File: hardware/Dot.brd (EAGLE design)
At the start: 25.4 x 31.5 mm, 43 parts, among them IC1 CAT24M010TS, IC2 SI1145, U1 ATMEGA328P-MU-QFN32, U2 TMP102, U3 ISL29125, U4 9DoF IMU, U5 BMP18

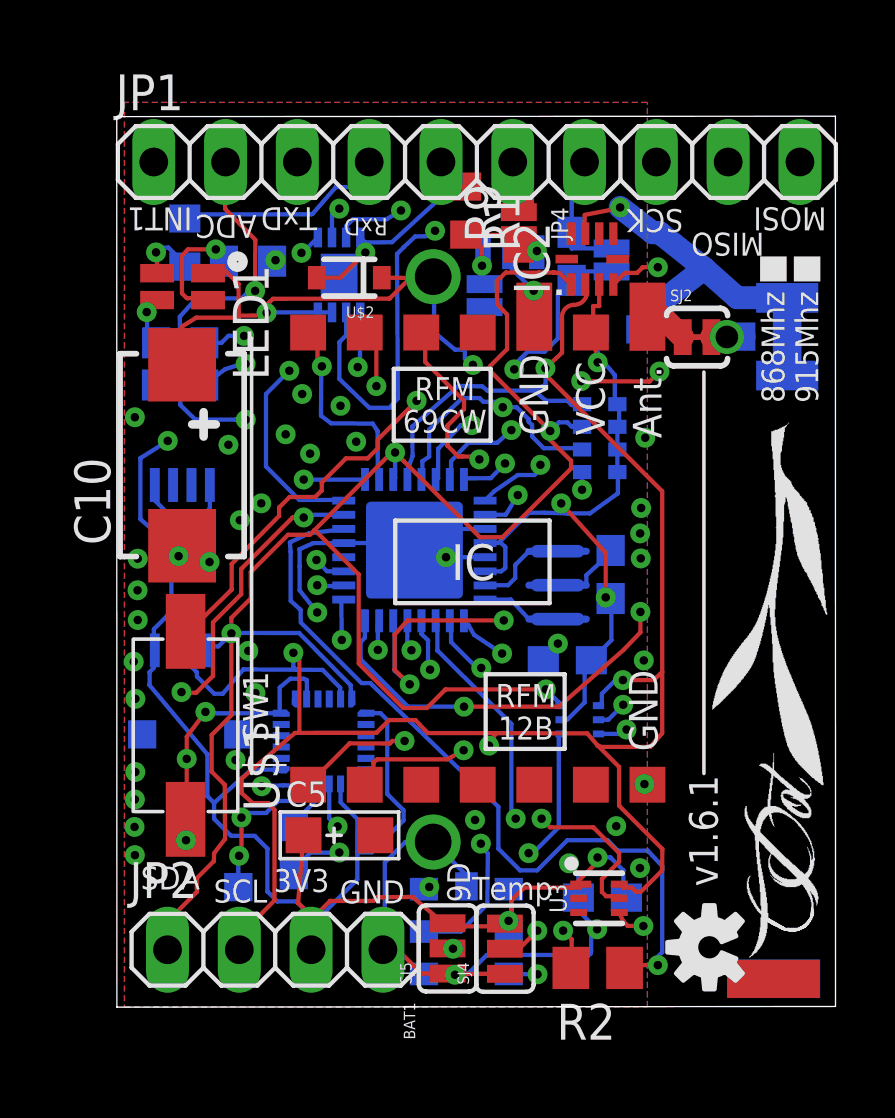
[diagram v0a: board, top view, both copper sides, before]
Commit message: Added MOSFET and pins for external on/off
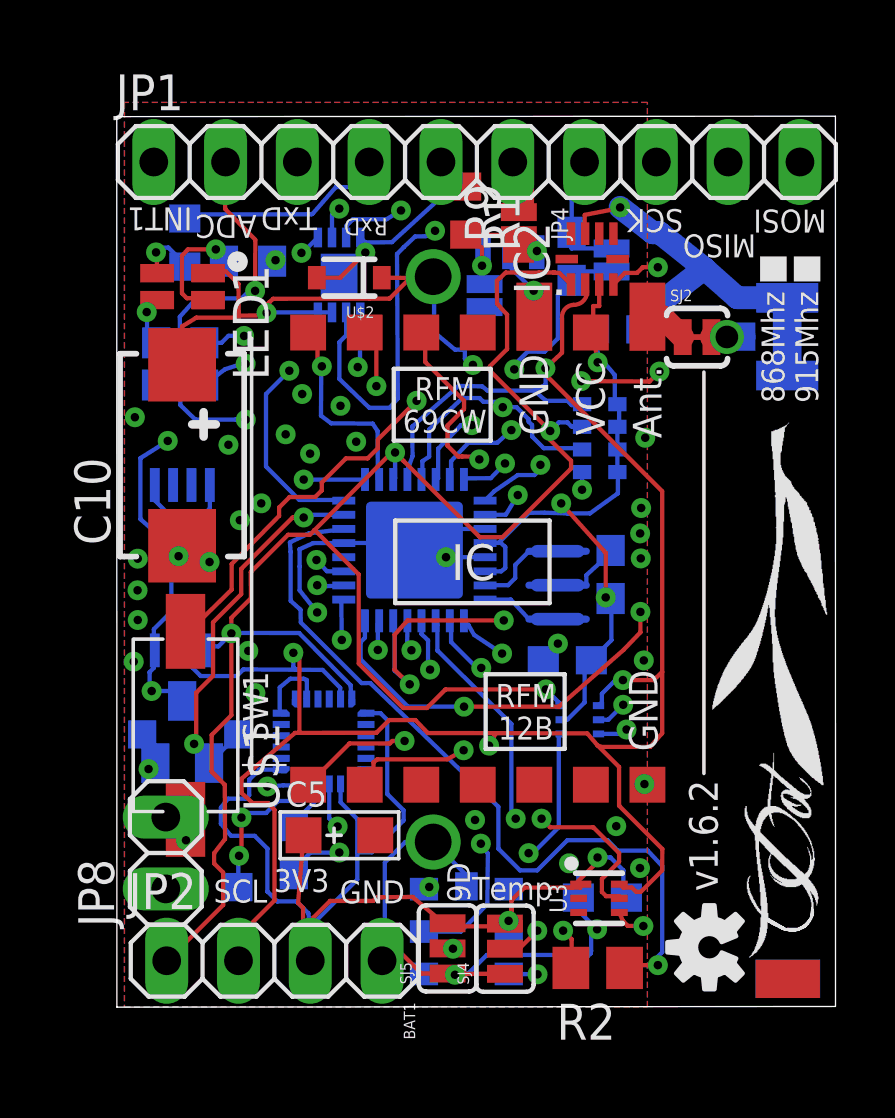
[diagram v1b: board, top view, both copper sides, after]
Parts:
- added JP8: (no value), pinhead:1X02
- added Q1: (no value), adafruit:SOT23
- moved JP2 0.39 mm to (5.93, 2.16)
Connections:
- new net N$16: JP8.1, Q1.2
- net +3V3: now also Q1.3
- net BUZZER: now also Q1.1
- net GND: now also JP8.2
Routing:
- net N$16: track 0.00 -> 13.3 mm, vias 0 -> 1
- net +3V3: track 144.0 -> 155.2 mm, vias 11 -> 12
- net GND: track 128.4 -> 118.2 mm, vias 46 -> 39
- net BUZZER: track 14.8 -> 13.6 mm, vias 3 -> 2
- net SDA: track 84.4 -> 85.0 mm
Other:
- board text added: "v1.6.2"
- board text removed: "SDA"
- board text removed: "v1.6.1"

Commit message: Moved Miso via away from the 4.7kOhm array, moved graphics further apart
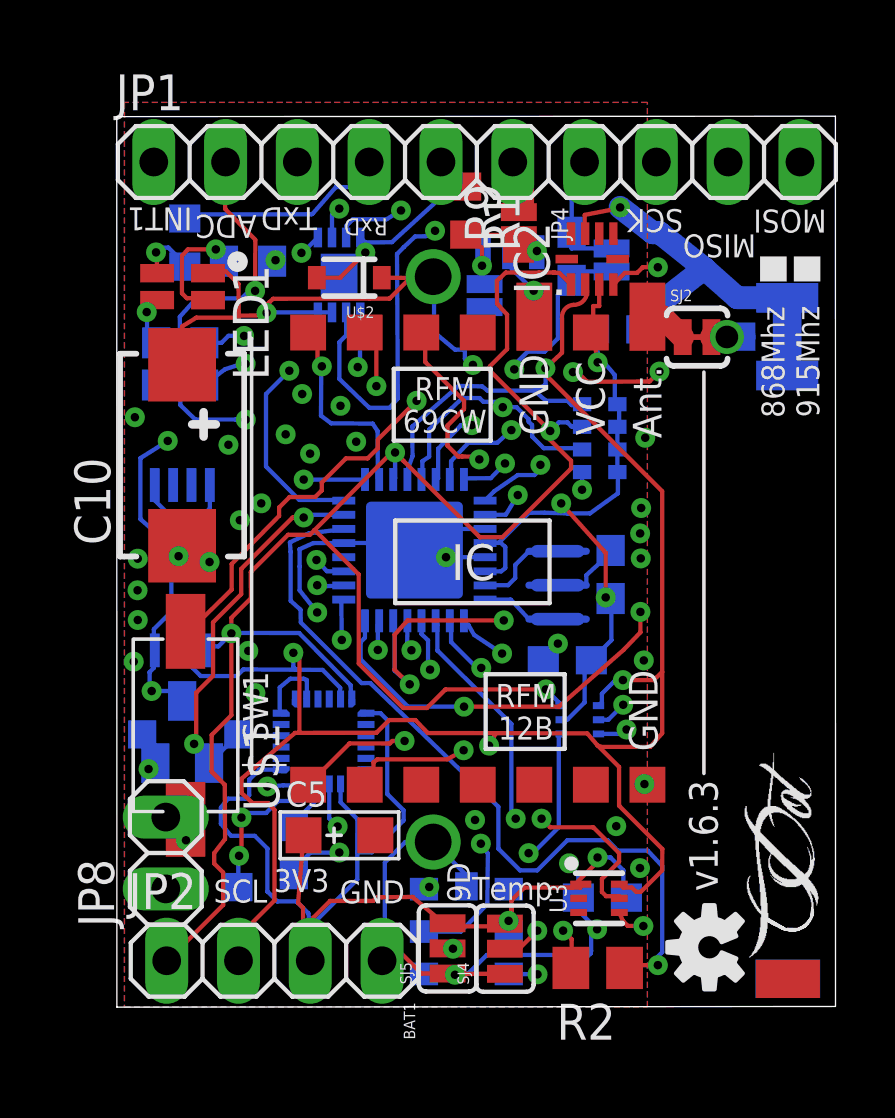
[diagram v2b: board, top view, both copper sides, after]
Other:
- board text added: "v1.6.3"
- board text removed: "v1.6.2"
